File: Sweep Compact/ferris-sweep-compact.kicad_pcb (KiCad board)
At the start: 2 copper layers, 107.2 x 86.9 mm, 21 parts, among them J1 MJ-4PP-9, SW10 SW_PUSH, SW11 SW_PUSH, SW12 SW_PUSH, SW14 SW_PUSH, SW15 SW_PUSH, SW16 SW_PUSH, SW17 SW_PUSH, SW18 SW_PUSH, SW2 SW_PUSH, SW20 SW_PUSH, SW21 SW_PUSH, SW3 SW_PUSH, SW4 SW_PUSH, SW5 SW_PUSH, SW6 SW_PUSH, SW8 SW_PUSH, SW9 SW_PUSH, U1 ProMicro

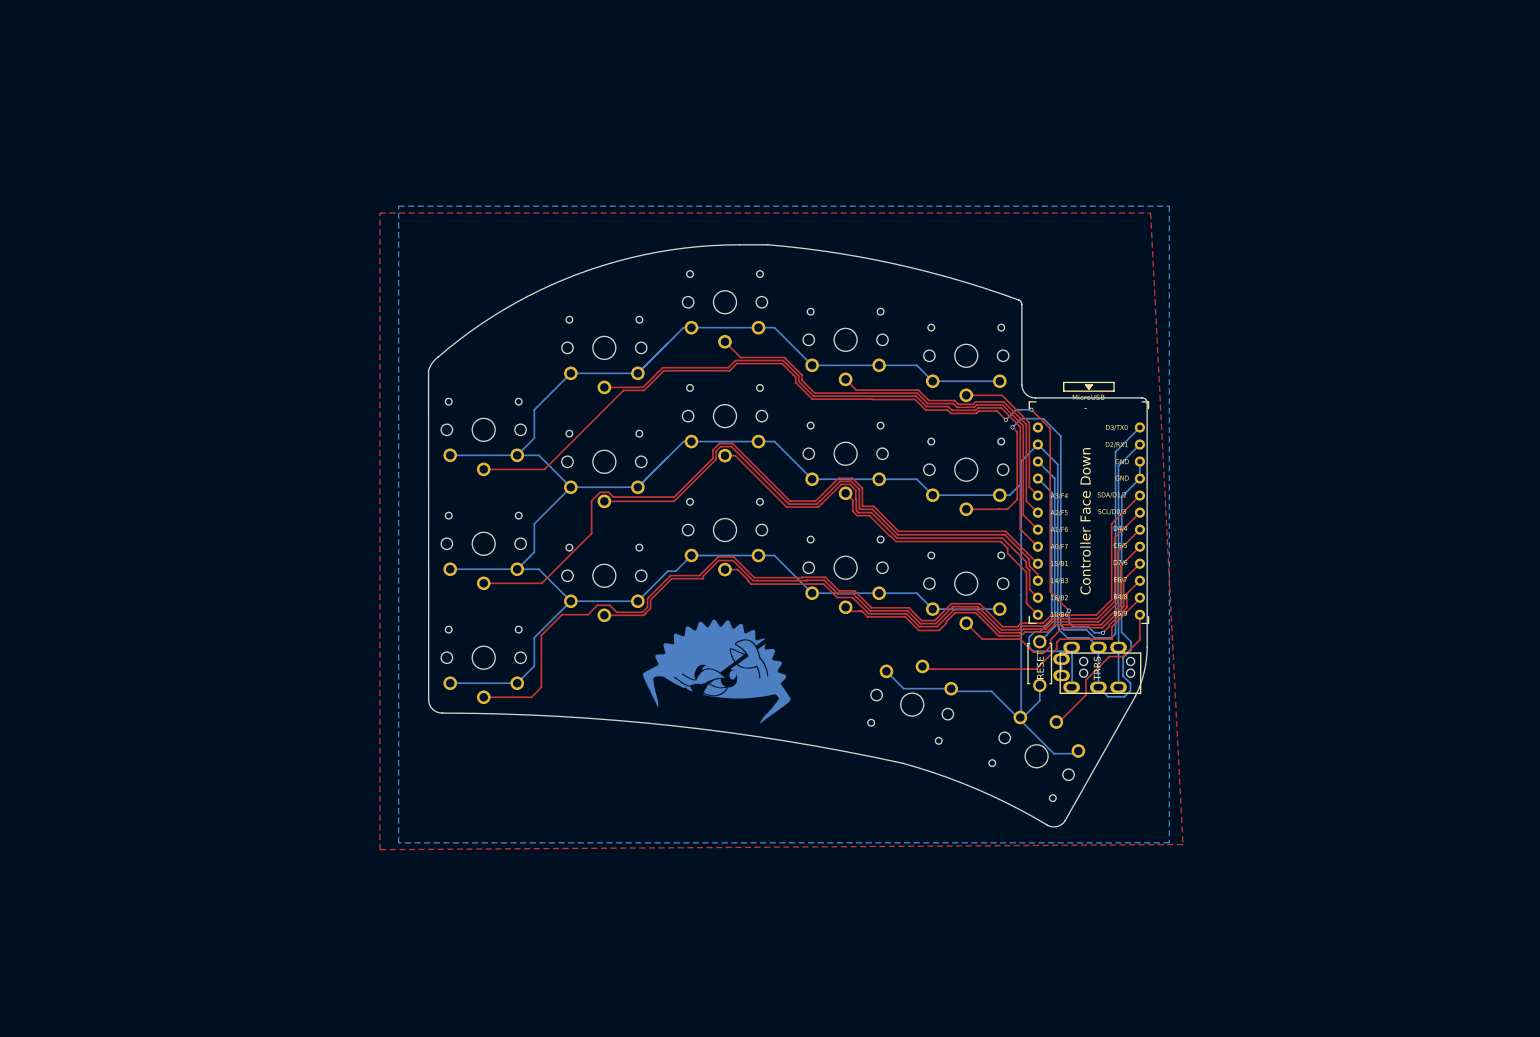
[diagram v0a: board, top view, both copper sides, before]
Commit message: Add files via upload
Edited Compact PCB cut out shape and added spider web artwork.
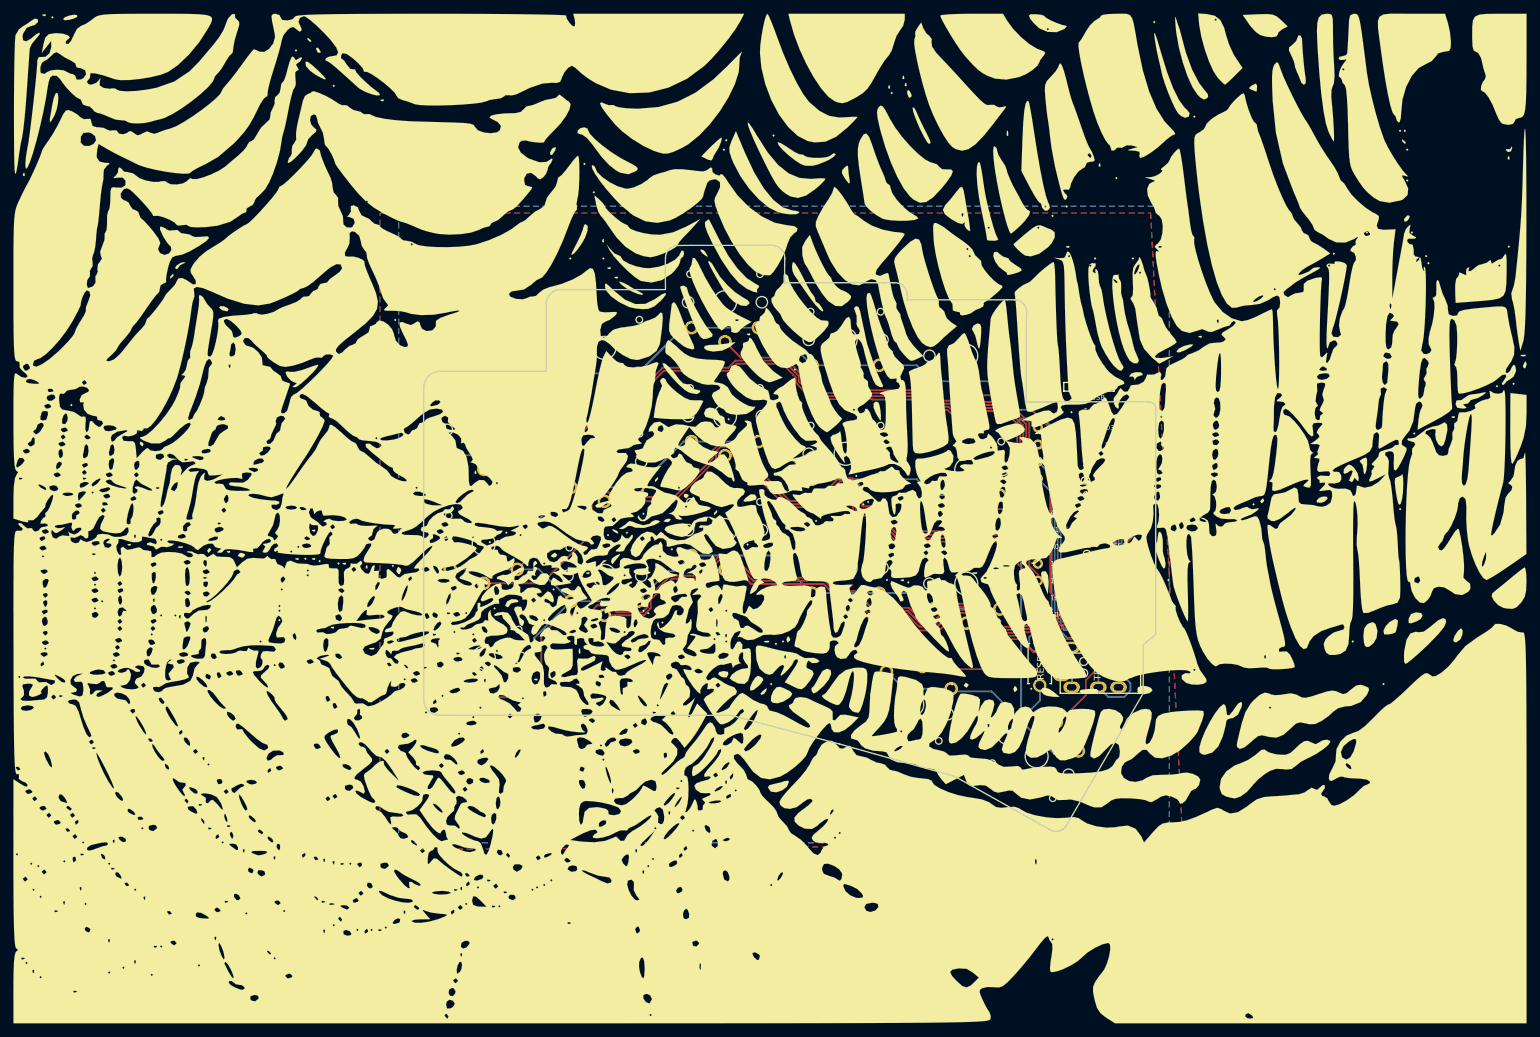
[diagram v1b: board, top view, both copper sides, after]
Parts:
- removed the G*** at (80.3, 79.5)
- added G***: LOGO, Desktop:web, B.Cu at (119.2, 33.6)
- added G***: LOGO, Desktop:web, F.Cu at (86.7, 55.8)
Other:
- board size 107.2 x 86.9 mm -> 109.2 x 87.5 mm
